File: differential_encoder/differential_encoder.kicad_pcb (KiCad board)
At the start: 2 copper layers, 92.7 x 52.8 mm, 43 parts, among them J101 Conn_01x12, J102 RJ45_LED_Shielded, J103 RJ45_LED_Shielded, Q101 Q_NMOS_GSD, Q102 Q_NMOS_GSD, Q103 Q_NMOS_GSD, Q104 Q_NMOS_GSD, Q105 Q_NMOS_GSD, Q106 Q_NMOS_GSD, U101 MAX489E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

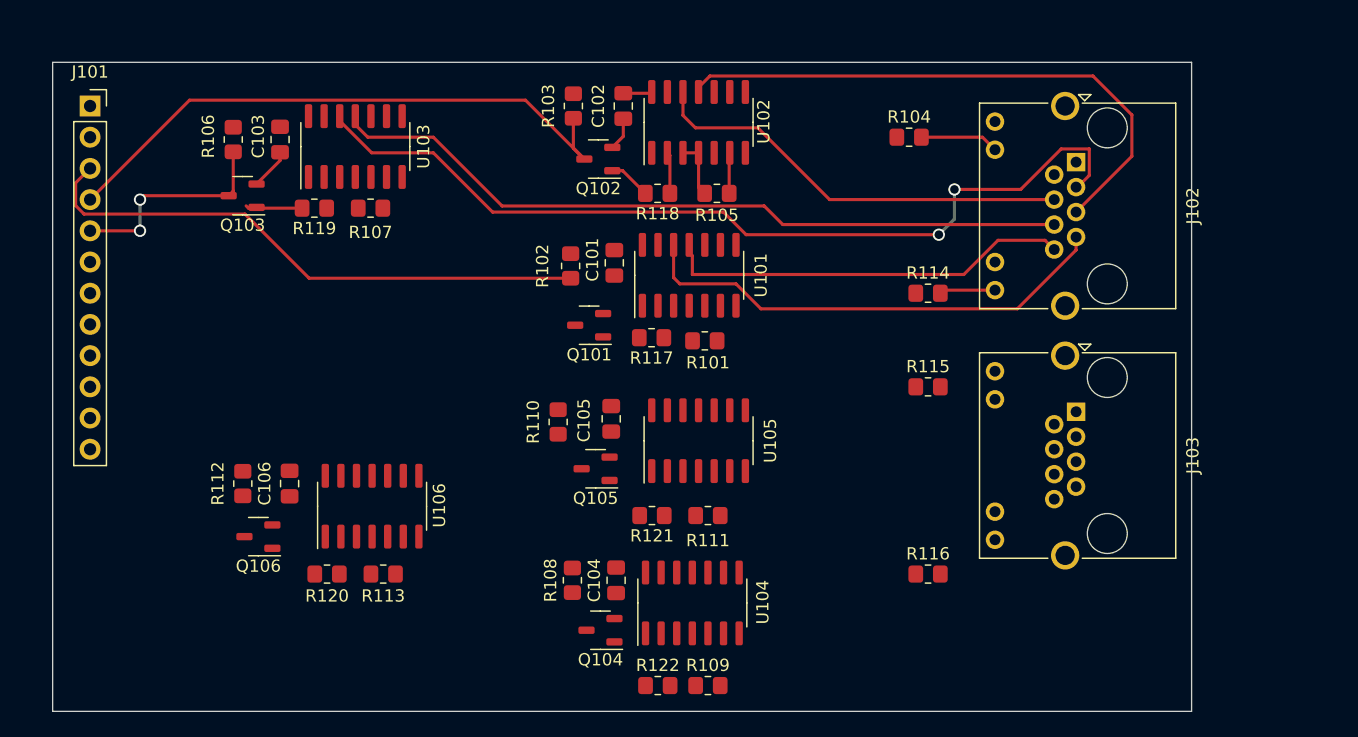
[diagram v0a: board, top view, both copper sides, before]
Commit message: first odrive board
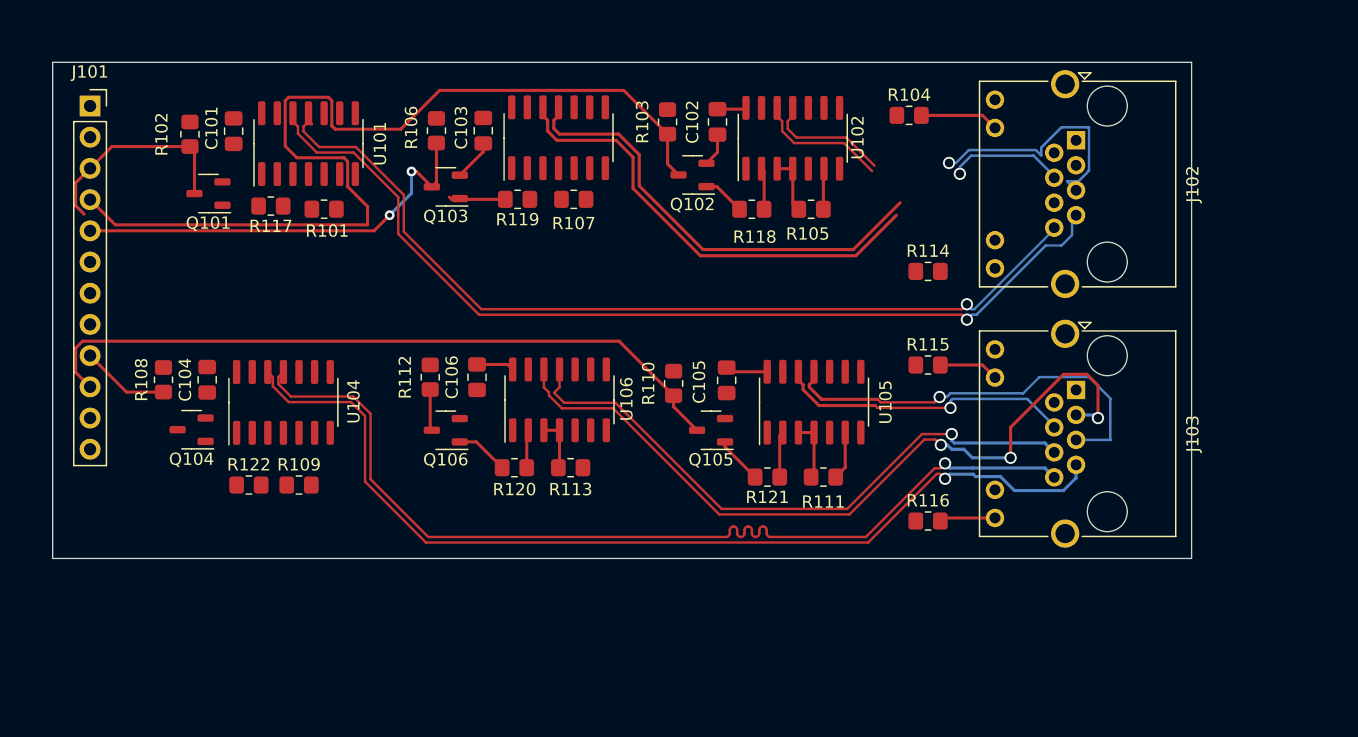
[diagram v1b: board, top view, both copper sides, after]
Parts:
- moved R109 37.1 mm to (95.7, 102.0)
- moved Q104 37.1 mm to (87.0, 97.5)
- moved R122 37.1 mm to (91.7, 102.0)
- moved U104 37.1 mm to (94.5, 95.2)
- moved C104 37.1 mm to (88.3, 93.4)
- moved R108 37.1 mm to (84.7, 93.4)
- moved C101 32.8 mm to (90.4, 73.2)
- moved Q101 32.8 mm to (88.4, 78.2)
- moved R102 32.8 mm to (86.9, 73.4)
- moved R117 32.8 mm to (93.5, 79.3)
- moved U101 32.8 mm to (96.5, 74.2)
- moved R101 32.8 mm to (97.8, 79.5)
- moved C106 17.5 mm to (110.2, 93.2)
- moved Q106 17.5 mm to (107.7, 97.5)
- moved R112 17.5 mm to (106.4, 93.2)
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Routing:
- net a0+: track 0.00 -> 80.1 mm, vias 0 -> 1
- net a0-: track 0.00 -> 79.3 mm, vias 0 -> 1
- net i0+: track 0.00 -> 63.6 mm, vias 0 -> 3
- net B0: track 0.00 -> 58.0 mm
- net i0-: track 0.00 -> 50.5 mm, vias 0 -> 1
- net a1-: track 33.4 -> 74.7 mm, vias 0 -> 1
- net a1+: track 39.5 -> 77.5 mm, vias 0 -> 1
- net i1+: track 73.2 -> 37.5 mm, vias 2 -> 0
- net b0-: track 0.00 -> 35.0 mm, vias 0 -> 1
- net B1: track 49.3 -> 78.5 mm
- net A1: track 46.3 -> 17.3 mm
- net b0+: track 0.00 -> 24.3 mm, vias 0 -> 1
- net i1-: track 61.0 -> 37.2 mm
- net I1: track 17.7 -> 35.1 mm
- net b1-: track 47.1 -> 30.5 mm, vias 0 -> 1
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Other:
- board size 92.7 x 52.8 mm -> 92.7 x 40.4 mm

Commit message: finished odrive layout
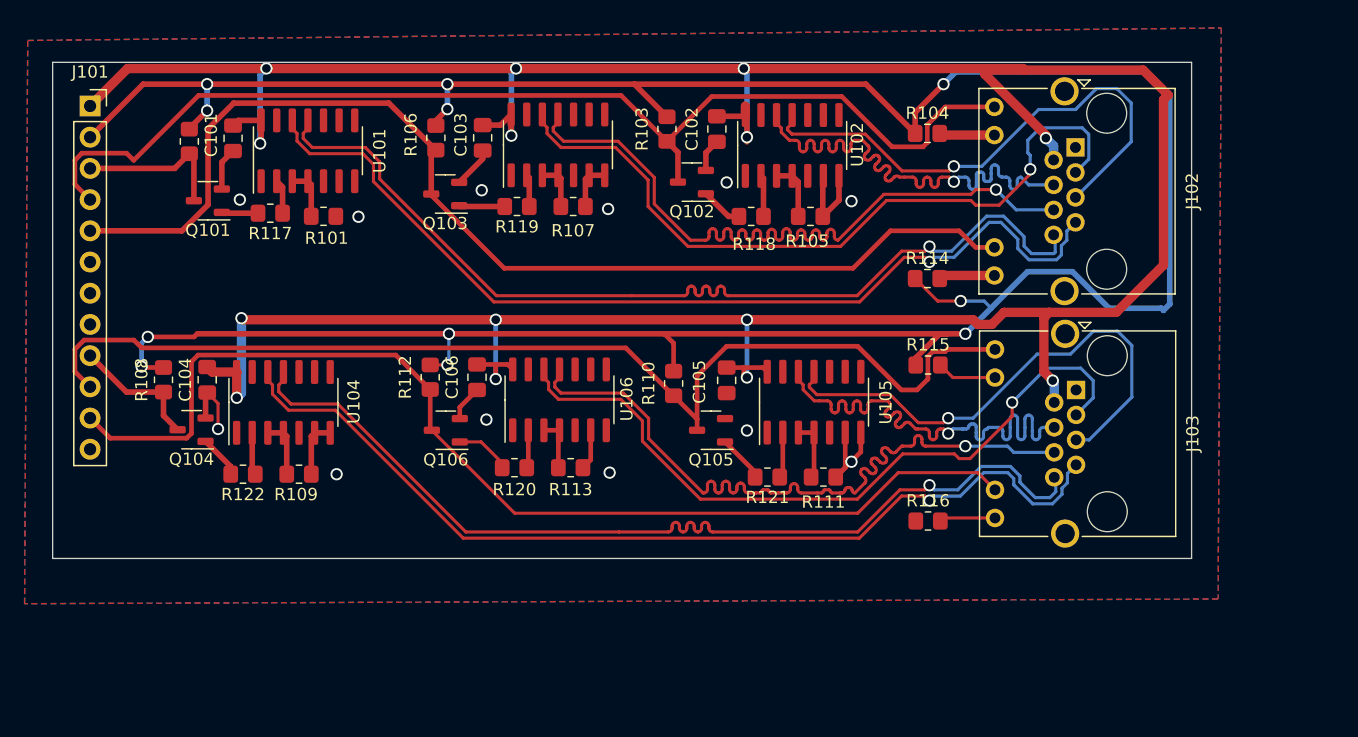
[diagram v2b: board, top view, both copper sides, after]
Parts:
- moved R104 2.09 mm to (146.9, 73.4)
- moved R122 1.00 mm to (91.2, 101.1), turned to 180 degrees
- moved R109 0.88 mm to (95.7, 101.1)
- moved C103 0.58 mm to (110.7, 73.7)
- moved R105 0.58 mm to (137.4, 80.1)
- moved R117 0.58 mm to (93.4, 79.8)
- moved R118 0.58 mm to (132.6, 80.1)
- moved R102 0.58 mm to (86.8, 74.0)
- moved R106 0.58 mm to (106.9, 73.7)
- moved U101 0.58 mm to (96.5, 74.8)
- moved U102 0.58 mm to (135.9, 74.3)
- moved C101 0.58 mm to (90.4, 73.8)
- moved C102 0.58 mm to (129.8, 73.0)
- moved J102 0.58 mm to (159.0, 74.5)
- moved Q101 0.58 mm to (88.3, 78.8)
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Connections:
- J102 pad 9: A1 -> B1
- J103 pad 11: I1 -> I0
- J103 pad 9: A1 -> B0
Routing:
- net +5V: track 8.88 -> 262.9 mm, vias 0 -> 14
- net +3V3: track 0.00 -> 233.9 mm, vias 0 -> 11
- net I0: track 3.37 -> 89.7 mm
- net I1: track 35.1 -> 91.6 mm, vias 2 -> 0
- net B0: track 58.0 -> 90.8 mm
- net GND: track 13.3 -> 45.5 mm, vias 0 -> 12
- net i1+: track 37.5 -> 60.9 mm, vias 0 -> 1
- net i1-: track 37.2 -> 60.4 mm, vias 0 -> 1
- net b1+: track 20.2 -> 43.0 mm
- net b0+: track 24.3 -> 42.2 mm
- net B1: track 78.5 -> 91.9 mm
- net b1-: track 30.5 -> 43.5 mm
- net i0-: track 50.5 -> 59.5 mm
- net b0-: track 35.0 -> 42.6 mm
- net A1: track 17.3 -> 12.6 mm
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- added copper zone on B.Cu, net GND
- added copper zone on F.Cu, net GND

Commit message: final version odrive
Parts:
- added R123: 10k, Resistor_SMD:R_0805_2012Metric_Pad1.20x1.40mm_HandSolder, F.Cu at (96.3, 71.6)
- added R124: 10k, Resistor_SMD:R_0805_2012Metric_Pad1.20x1.40mm_HandSolder, F.Cu at (92.2, 71.6)
- added R125: 10k, Resistor_SMD:R_0805_2012Metric_Pad1.20x1.40mm_HandSolder, F.Cu at (104.6, 76.7)
- added R126: 10k, Resistor_SMD:R_0805_2012Metric_Pad1.20x1.40mm_HandSolder, F.Cu at (101.6, 77.7)
- added R127: 10k, Resistor_SMD:R_0805_2012Metric_Pad1.20x1.40mm_HandSolder, F.Cu at (101.6, 75.4)
- added R128: 10k, Resistor_SMD:R_0805_2012Metric_Pad1.20x1.40mm_HandSolder, F.Cu at (139.9, 71.6)
- added R129: 10k, Resistor_SMD:R_0805_2012Metric_Pad1.20x1.40mm_HandSolder, F.Cu at (144.0, 71.6)
- added R130: 10k, Resistor_SMD:R_0805_2012Metric_Pad1.20x1.40mm_HandSolder, F.Cu at (149.3, 77.7)
- added R131: 10k, Resistor_SMD:R_0805_2012Metric_Pad1.20x1.40mm_HandSolder, F.Cu at (149.3, 75.4)
- added R132: 10k, Resistor_SMD:R_0805_2012Metric_Pad1.20x1.40mm_HandSolder, F.Cu at (152.4, 76.7)
- added R133: 10k, Resistor_SMD:R_0805_2012Metric_Pad1.20x1.40mm_HandSolder, F.Cu at (117.1, 71.6)
- added R134: 10k, Resistor_SMD:R_0805_2012Metric_Pad1.20x1.40mm_HandSolder, F.Cu at (121.2, 71.6)
- added R135: 10k, Resistor_SMD:R_0805_2012Metric_Pad1.20x1.40mm_HandSolder, F.Cu at (126.5, 77.7)
- added R136: 10k, Resistor_SMD:R_0805_2012Metric_Pad1.20x1.40mm_HandSolder, F.Cu at (126.5, 75.4)
- added R137: 10k, Resistor_SMD:R_0805_2012Metric_Pad1.20x1.40mm_HandSolder, F.Cu at (129.5, 76.7)
- added R138: 10k, Resistor_SMD:R_0805_2012Metric_Pad1.20x1.40mm_HandSolder, F.Cu at (92.3, 91.1)
- added R139: 10k, Resistor_SMD:R_0805_2012Metric_Pad1.20x1.40mm_HandSolder, F.Cu at (96.3, 91.1)
- added R140: 10k, Resistor_SMD:R_0805_2012Metric_Pad1.20x1.40mm_HandSolder, F.Cu at (101.7, 97.2)
- added R141: 10k, Resistor_SMD:R_0805_2012Metric_Pad1.20x1.40mm_HandSolder, F.Cu at (101.7, 94.9)
- added R142: 10k, Resistor_SMD:R_0805_2012Metric_Pad1.20x1.40mm_HandSolder, F.Cu at (104.7, 96.2)
- added R143: 10k, Resistor_SMD:R_0805_2012Metric_Pad1.20x1.40mm_HandSolder, F.Cu at (140.0, 91.1)
- added R144: 10k, Resistor_SMD:R_0805_2012Metric_Pad1.20x1.40mm_HandSolder, F.Cu at (144.0, 91.1)
- added R145: 10k, Resistor_SMD:R_0805_2012Metric_Pad1.20x1.40mm_HandSolder, F.Cu at (149.4, 97.2)
- added R146: 10k, Resistor_SMD:R_0805_2012Metric_Pad1.20x1.40mm_HandSolder, F.Cu at (149.4, 94.9)
- added R147: 10k, Resistor_SMD:R_0805_2012Metric_Pad1.20x1.40mm_HandSolder, F.Cu at (152.4, 96.2)
- added R148: 10k, Resistor_SMD:R_0805_2012Metric_Pad1.20x1.40mm_HandSolder, F.Cu at (117.1, 91.1)
- added R149: 10k, Resistor_SMD:R_0805_2012Metric_Pad1.20x1.40mm_HandSolder, F.Cu at (121.2, 91.1)
- added R150: 10k, Resistor_SMD:R_0805_2012Metric_Pad1.20x1.40mm_HandSolder, F.Cu at (126.5, 97.2)
- added R151: 10k, Resistor_SMD:R_0805_2012Metric_Pad1.20x1.40mm_HandSolder, F.Cu at (126.5, 94.9)
- added R152: 10k, Resistor_SMD:R_0805_2012Metric_Pad1.20x1.40mm_HandSolder, F.Cu at (129.5, 96.2)
- moved R114 8.81 mm to (155.7, 84.8)
- moved R104 8.80 mm to (155.7, 73.4)
- moved R103 8.58 mm to (134.1, 74.7)
- moved R110 7.89 mm to (134.1, 94.2)
- moved Q102 7.78 mm to (135.4, 78.7)
- moved J103 7.77 mm to (166.8, 94.1)
- moved J102 7.77 mm to (166.7, 74.5)
- moved R115 7.77 mm to (154.7, 92.2)
- moved R116 7.77 mm to (154.7, 104.9)
- moved U102 6.96 mm to (142.5, 76.5)
- moved C102 6.85 mm to (136.4, 74.7)
- moved R105 6.85 mm to (144.0, 81.8)
- moved R118 6.85 mm to (139.2, 81.8)
- moved Q105 6.14 mm to (135.4, 98.2)
- moved C105 5.89 mm to (136.4, 94.2)
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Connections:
- U101 pad 11: a1- -> Net-(U101-B)
- U101 pad 12: a1+ -> Net-(U101-A)
- U102 pad 11: b1- -> Net-(U102-B)
- U102 pad 12: b1+ -> Net-(U102-A)
- U103 pad 11: i1- -> Net-(U103-B)
- U103 pad 12: i1+ -> Net-(U103-A)
- U104 pad 11: a0- -> Net-(U104-B)
- U104 pad 12: a0+ -> Net-(U104-A)
- U105 pad 11: b0- -> Net-(U105-B)
- U105 pad 12: b0+ -> Net-(U105-A)
- U106 pad 11: i0- -> Net-(U106-B)
- U106 pad 12: i0+ -> Net-(U106-A)
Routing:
- net +3V3: track 233.9 -> 312.0 mm, vias 11 -> 15
- net +5V: track 262.9 -> 282.4 mm
- net I0: track 89.7 -> 103.6 mm
- net GND: track 45.5 -> 32.0 mm, vias 12 -> 18
- net Net-(U103-A): track 0.00 -> 12.6 mm
- net B1: track 91.9 -> 104.1 mm
- net Net-(U106-A): track 0.00 -> 12.2 mm
- net Net-(U101-A): track 0.00 -> 11.8 mm
- net Net-(U102-A): track 0.00 -> 11.7 mm
- net Net-(U104-A): track 0.00 -> 11.7 mm
- net Net-(U105-A): track 0.00 -> 11.5 mm
- net I1: track 91.6 -> 102.6 mm
- net Net-(U104-B): track 0.00 -> 9.35 mm
- net Net-(U106-B): track 0.00 -> 9.34 mm
- net Net-(U105-B): track 0.00 -> 9.34 mm
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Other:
- board size 92.7 x 40.4 mm -> 99.8 x 40.4 mm

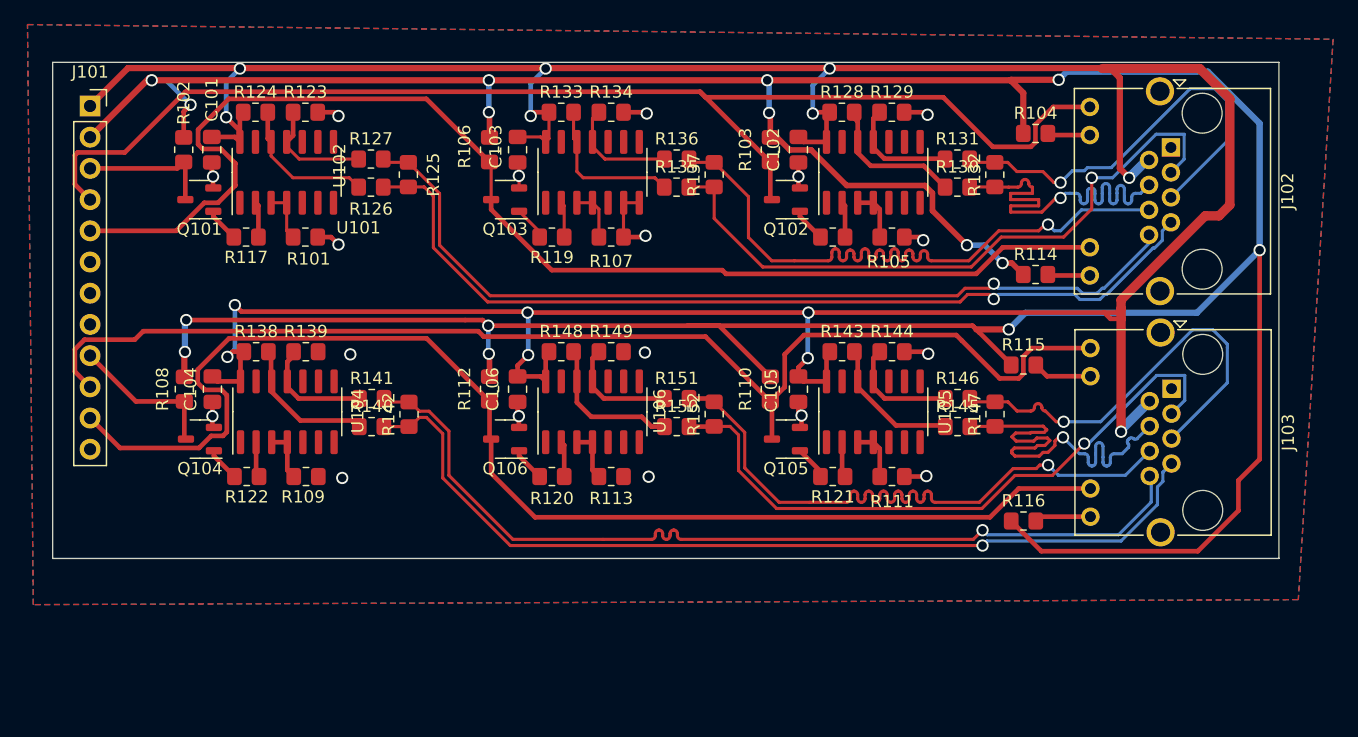
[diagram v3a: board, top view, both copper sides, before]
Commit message: odrive traces are now chunky
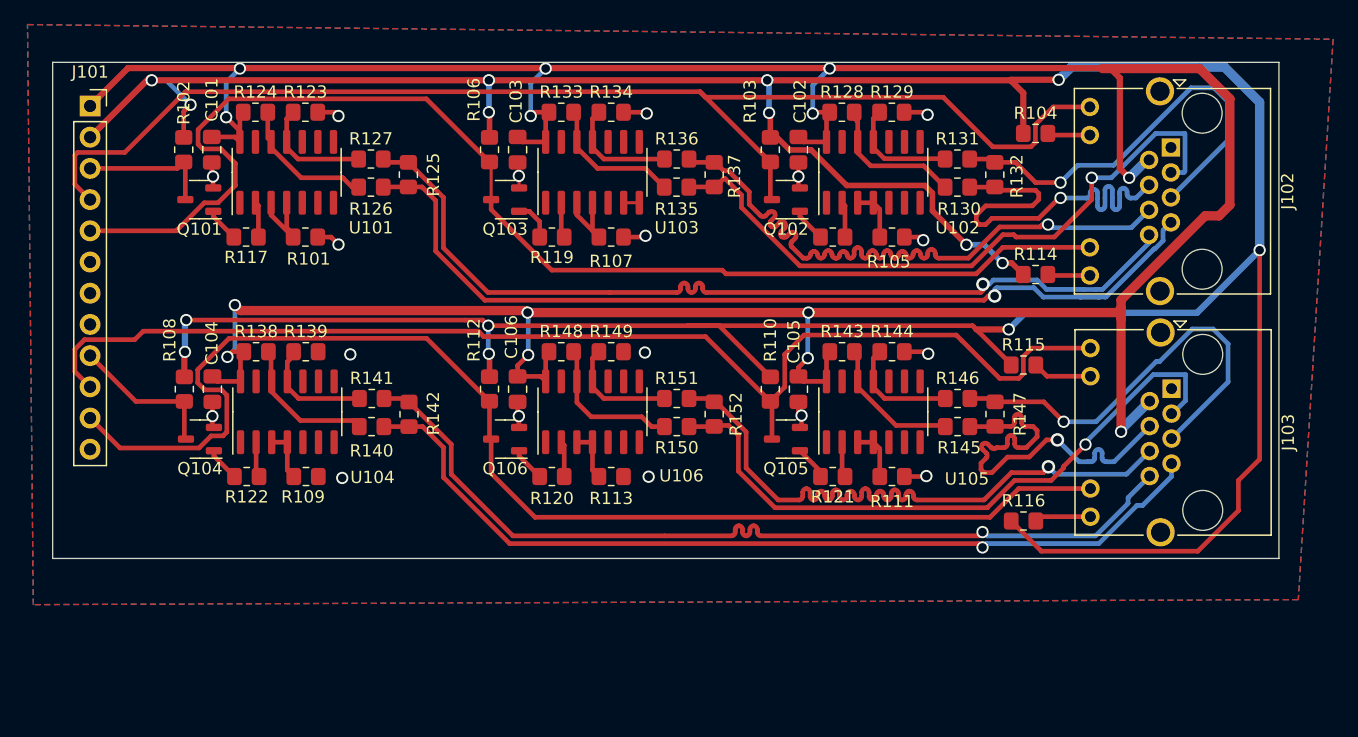
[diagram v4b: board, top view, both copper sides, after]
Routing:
- net GND: track 32.0 -> 29.2 mm
- net a1-: track 72.7 -> 75.2 mm
- net Net-(U103-DE): track 4.28 -> 6.55 mm
- net Net-(U101-DE): track 4.28 -> 6.55 mm
- net +5V: track 282.4 -> 280.5 mm
- net a0-: track 75.0 -> 73.1 mm
- net a0+: track 74.9 -> 73.1 mm
- net Net-(U103-A): track 12.6 -> 11.0 mm
- net +3V3: track 312.0 -> 313.3 mm
- net Net-(U101-A): track 11.8 -> 11.1 mm
- net b0+: track 35.4 -> 34.7 mm
